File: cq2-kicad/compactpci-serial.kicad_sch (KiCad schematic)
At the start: 55 parts, among them P1 AirMax VS 6W, U1 74LVC2G125, U2 PCA9554A, U3 PCA9546A, U4 24LC02B, U5 MPM3650

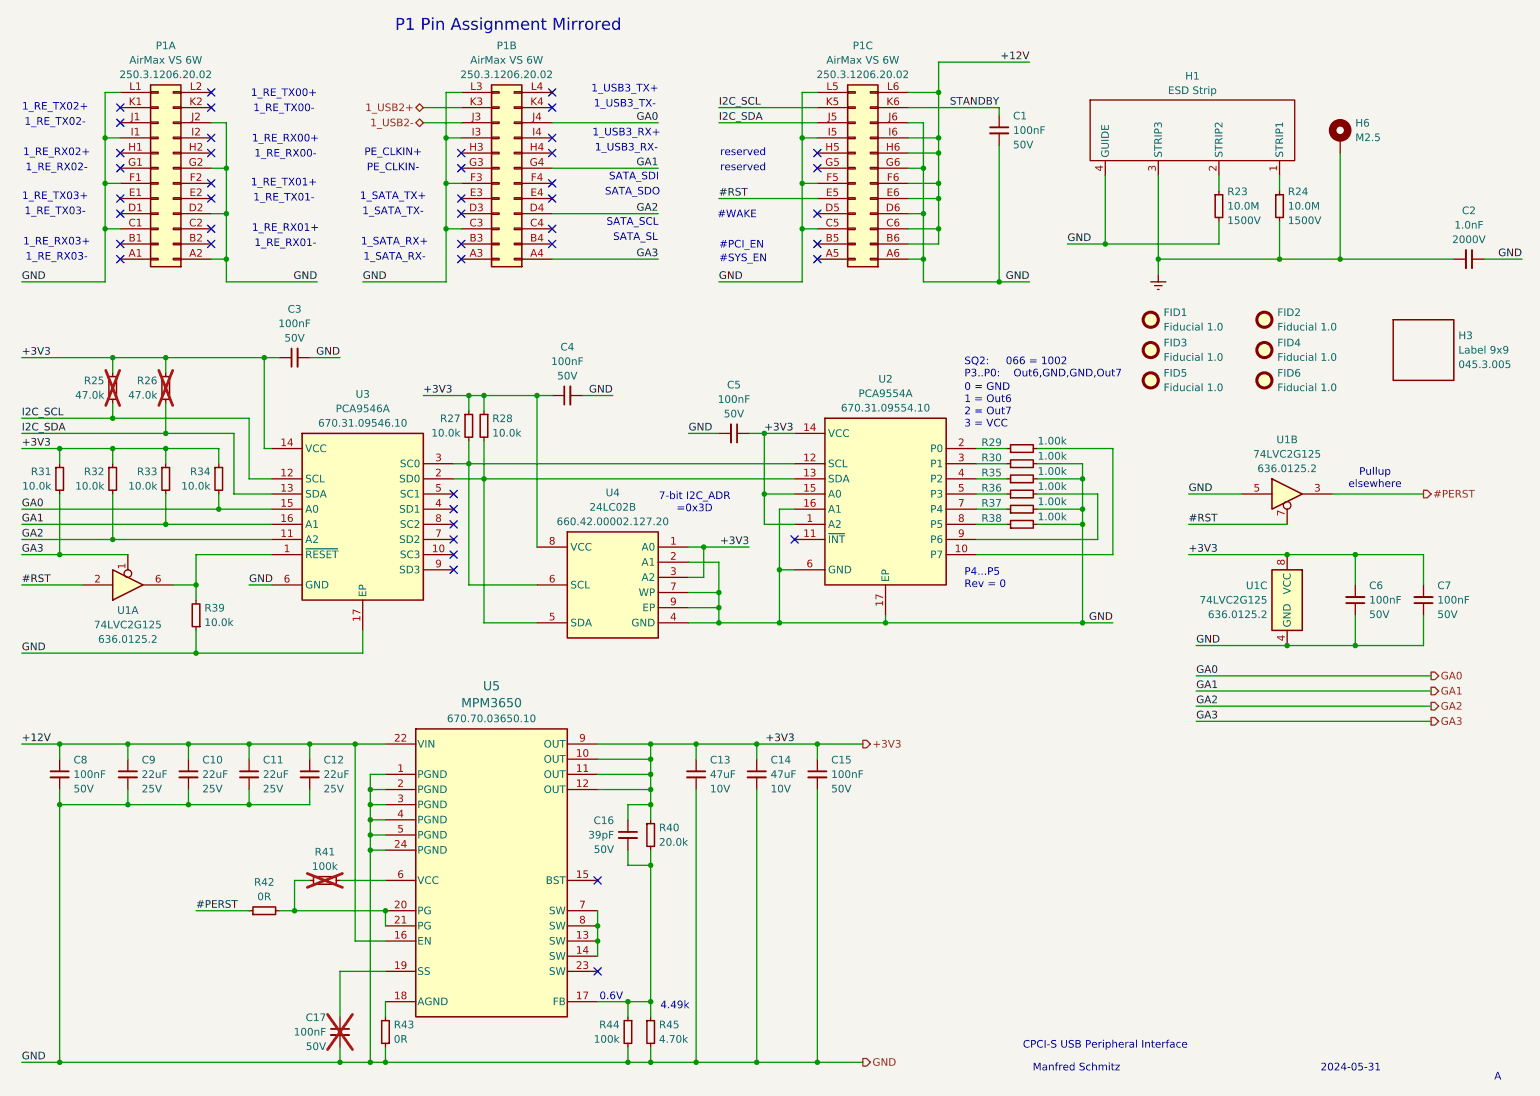
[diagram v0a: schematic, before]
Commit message: drc checked before panalization
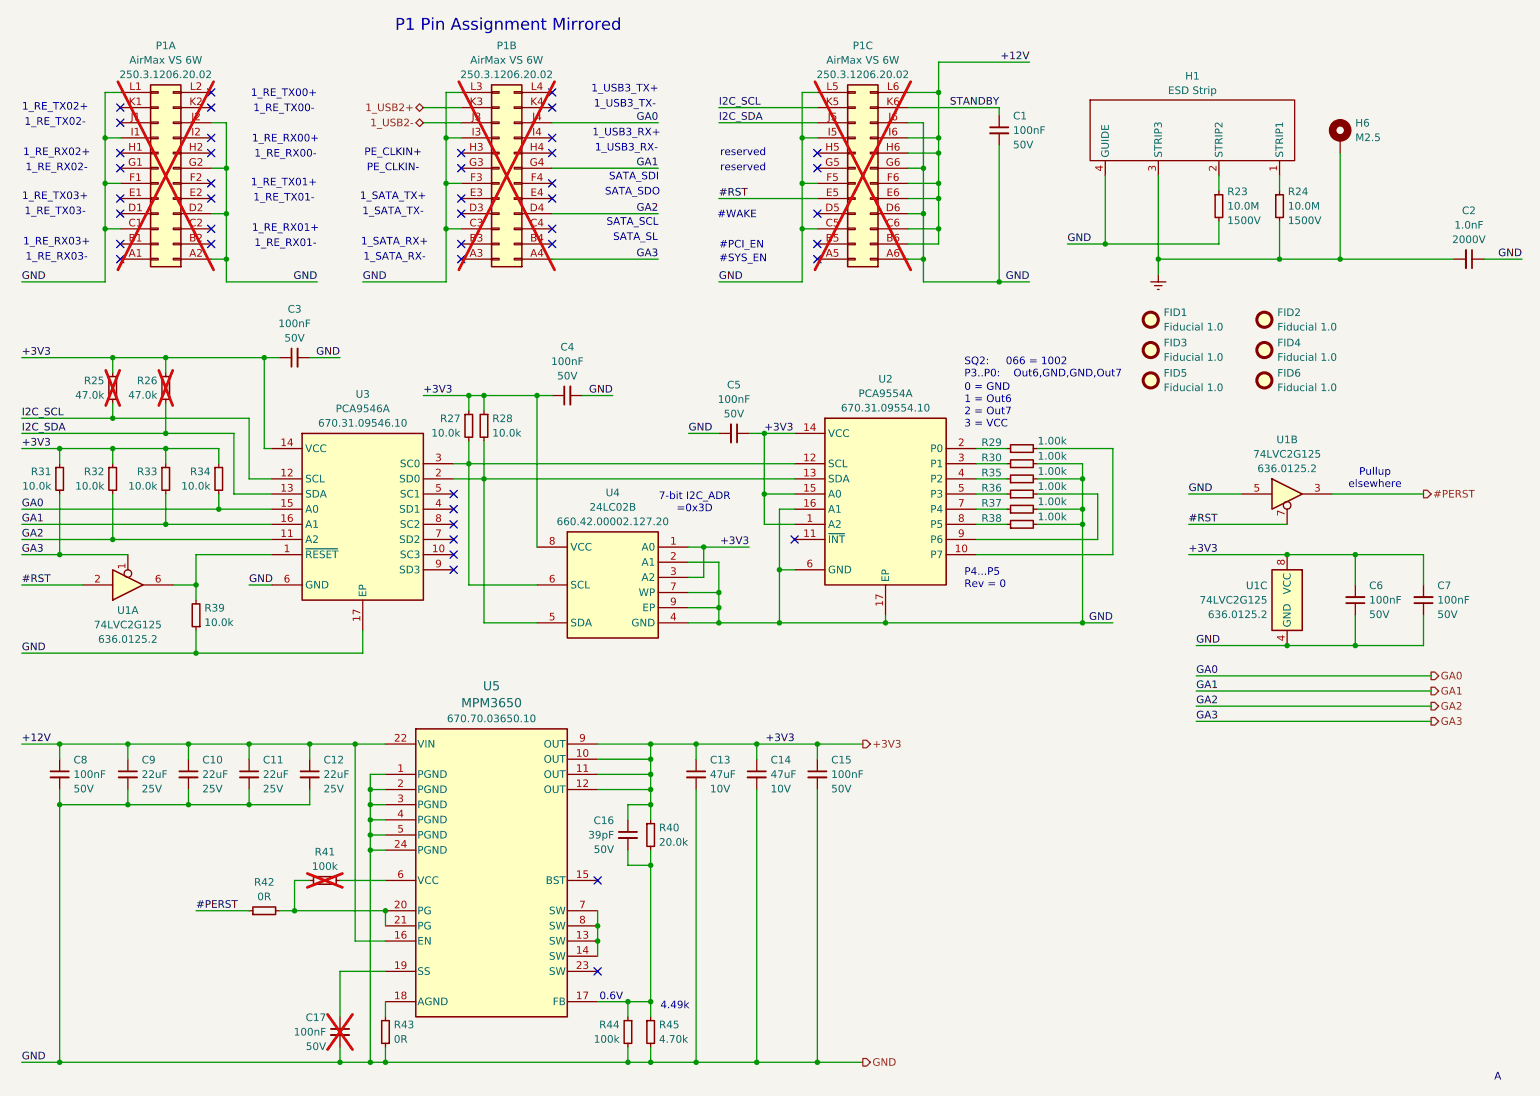
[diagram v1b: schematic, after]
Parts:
- removed H3: Label 9x9, 1-special:various-18, symbol ci4rail-database:various/18
- P1: now not fitted
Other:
- note removed: "2024-05-31"
- note removed: "CPCI-S USB Peripheral Interface"
- note removed: "Manfred Schmitz"
- title: (none) -> CQ2
